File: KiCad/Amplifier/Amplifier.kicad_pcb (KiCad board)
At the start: 2 copper layers, 46 x 56 mm, 29 parts, among them J1 Screw_Terminal_01x03, J2 Screw_Terminal_01x03, Q1 NPN, Q2 NPN, U1 TL074

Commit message: removed unnecessary buffer before filter's output
this drops the number of op amps from 5 to 4, allowing us to use 1 IC instead of 2 ICs with 3 unused circuits.
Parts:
- R10, R9: footprint Resistor_THT:R_Axial_DIN0207_L6.3mm_D2.5mm_P7.62mm_Horizontal -> Resistor_SMD:R_0805_2012Metric
- moved R9 2.99 mm to (83.9, 70.4), turned to 0 degrees
- moved R10 2.79 mm to (83.9, 60.3), turned to 0 degrees
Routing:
- net -9V: track 60.1 -> 53.8 mm
- net GND: track 12.0 -> 16.0 mm, vias 2 -> 4
- net Net-(D2-K): track 4.66 -> 3.01 mm
- net Net-(D1-K): track 3.52 -> 4.19 mm

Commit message: filter pcb layout done
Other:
- board text added: "+9V"
- board text added: "-9V"
- board text added: "Amplifier"
- board text removed: "Oscillator"
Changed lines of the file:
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@@
 			(font
 				(size 1 1)
-				(thickness 0.12)
+				(thickness 0.15)
 			)
 			(justify left bottom)
@@
 			(font
 				(size 1 1)
-				(thickness 0.12)
+				(thickness 0.15)
 			)
 			(justify left bottom)
@@
 			(font
 				(size 1 1)
-				(thickness 0.12)
+				(thickness 0.15)
+			)
+			(justify left bottom)
+		)
+	)
+	(gr_text "-9V"
+		(at 75.5 57 0)
+		(layer "F.SilkS")
+		(effects
+			(font
+				(size 1 1)
+				(thickness 0.15)
+			)
+			(justify left bottom)
+		)
+	)
+	(gr_text "+9V"
+		(at 75.5 72 0)
+		(layer "F.SilkS")
+		(effects
+			(font
+				(size 1 1)
+				(thickness 0.15)
 			)
 			(justify left bottom)
@@
 			(font
 				(size 1 1)
-				(thickness 0.12)
+				(thickness 0.15)
 			)
 			(justify left bottom)
 		)
 	)
-	(gr_text "Oscillator"
-		(at 47.4 70.8 90)
+	(gr_text "Amplifier"
+		(at 48.5 73 90)
 		(layer "F.SilkS")
 		(effects
 			(font
-				(size 2 2)
-				(thickness 0.23)
+				(size 3 3)
+				(thickness 0.45)
 			)
 			(justify left bottom)

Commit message: oscillator pcb layout done
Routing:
- net +9V: track 41.4 -> 46.5 mm
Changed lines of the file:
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@@
+	)
+	(segment
+		(start 73 69)
+		(end 74.5 67.5)
+		(width 0.5)
+		(layer "F.Cu")
+		(net "+9V")
+	)
+	(segment
+		(start 74.5 67.5)
+		(end 77.46 67.5)
+		(width 0.5)
+		(layer "F.Cu")
+		(net "+9V")
 	)
 	(segment

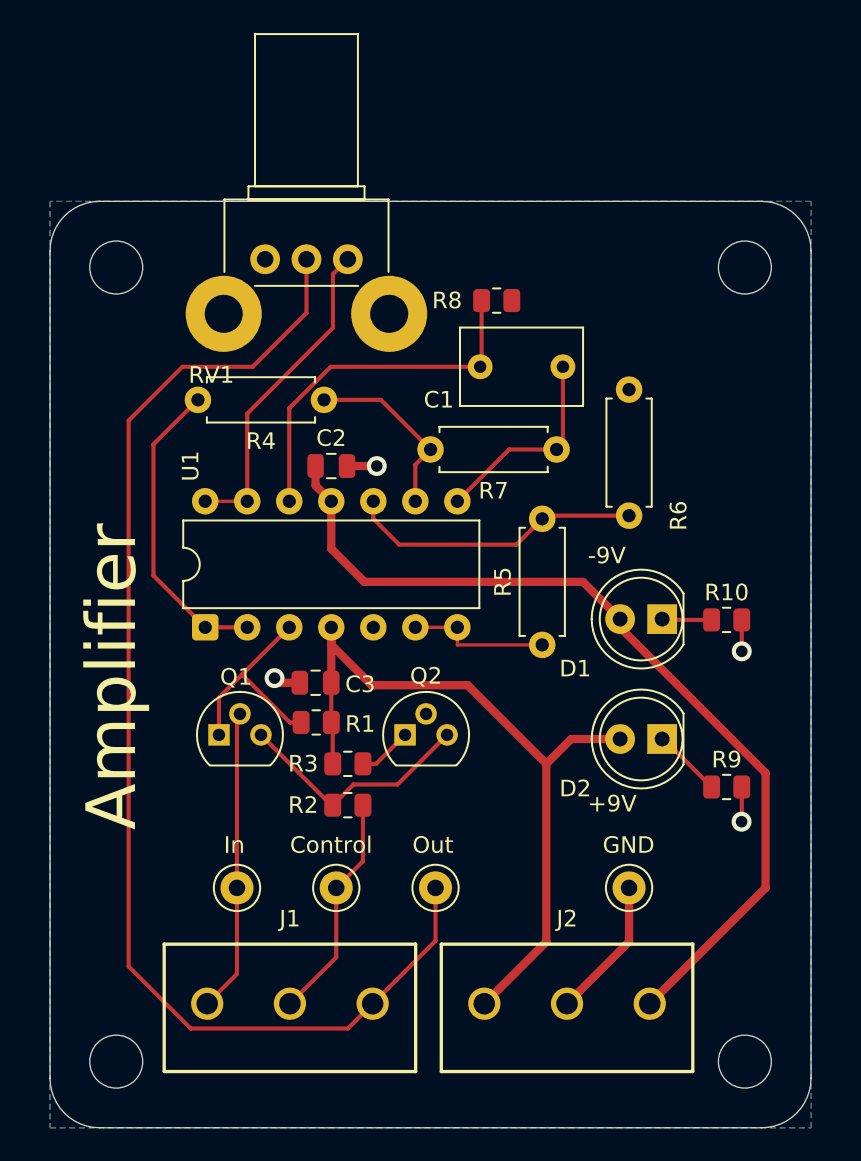
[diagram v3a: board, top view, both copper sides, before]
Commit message: power pcb layout done
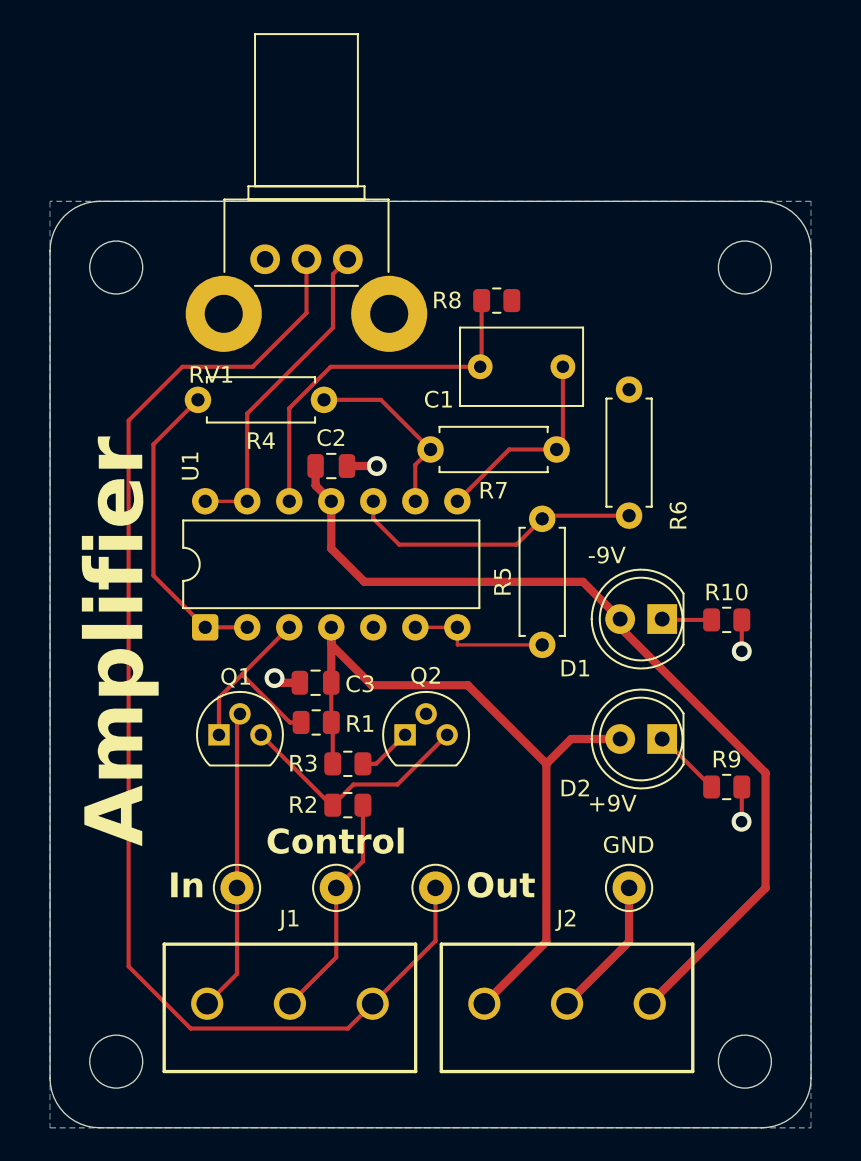
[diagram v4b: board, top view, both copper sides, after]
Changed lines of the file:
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@@
 		(layer "Edge.Cuts")
-	)
-	(gr_text "In"
-		(at 53.5 74.5 0)
-		(layer "F.SilkS")
-		(effects
-			(font
-				(size 1 1)
-				(thickness 0.15)
-			)
-			(justify left bottom)
-		)
-	)
-	(gr_text "Control"
-		(at 57.5 74.5 0)
-		(layer "F.SilkS")
-		(effects
-			(font
-				(size 1 1)
-				(thickness 0.15)
-			)
-			(justify left bottom)
-		)
-	)
-	(gr_text "Out"
-		(at 64.9 74.5 0)
-		(layer "F.SilkS")
-		(effects
-			(font
-				(size 1 1)
-				(thickness 0.15)
-			)
-			(justify left bottom)
-		)
 	)
 	(gr_text "-9V"
@@
 		)
 	)
-	(gr_text "Amplifier"
-		(at 48.5 73 90)
+	(gr_text "In"
+		(at 51.25 77.25 0)
 		(layer "F.SilkS")
 		(effects
 			(font
-				(size 3 3)
-				(thickness 0.45)
+				(size 1.5 1.5)
+				(thickness 0.3)
+				(bold yes)
+			)
+			(justify bottom)
+		)
+	)
+	(gr_text "Control"
+		(at 60.3 74.6 0)
+		(layer "F.SilkS")
+		(effects
+			(font
+				(size 1.5 1.5)
+				(thickness 0.3)
+				(bold yes)
+			)
+			(justify bottom)
+		)
+	)
+	(gr_text "Out"
+		(at 70.25 77.25 0)
+		(layer "F.SilkS")
+		(effects
+			(font
+				(size 1.5 1.5)
+				(thickness 0.3)
+				(bold yes)
+			)
+			(justify bottom)
+		)
+	)
+	(gr_text "Amplifier"
+		(at 49 74 90)
+		(layer "F.SilkS")
+		(effects
+			(font
+				(size 3.5 3.5)
+				(thickness 0.7)
+				(bold yes)
 			)
 			(justify left bottom)

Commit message: added mounting holes to schematics, adjusted board sizes
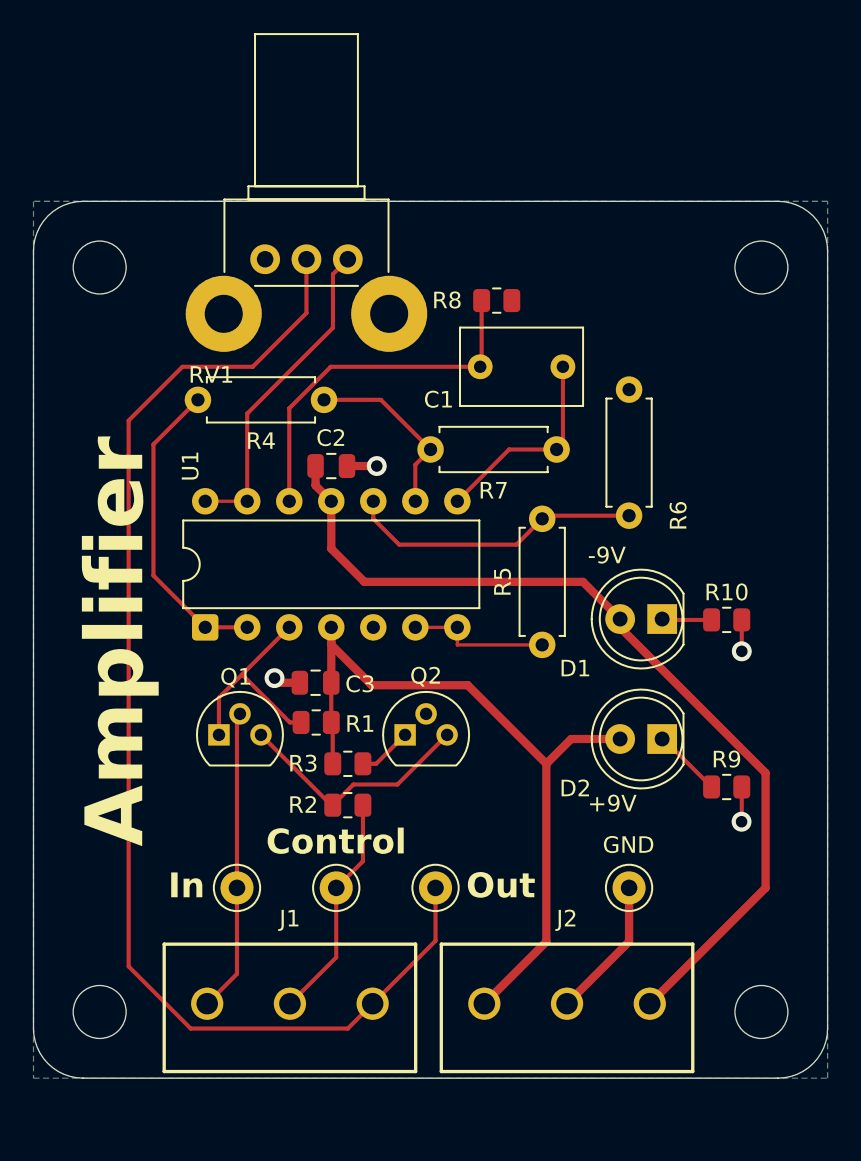
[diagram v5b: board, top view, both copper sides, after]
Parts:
- moved H2 3.16 mm to (46.0, 84.0)
- moved H3 3.16 mm to (86.0, 84.0)
- moved H1 1.00 mm to (46.0, 39.0)
- moved H4 1.00 mm to (86.0, 39.0)
- renumbered REF** to H1, REF** to H2, REF** to H3, REF** to H4
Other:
- board size 46 x 56 mm -> 48 x 53 mm
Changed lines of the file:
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@@
 	(footprint "MountingHole:MountingHole_3.2mm_M3"
 		(layer "F.Cu")
-		(at 47 87)
+		(at 46 84)
 		(descr "Mounting Hole 3.2mm, M3, no annular, generated by kicad-footprint-generator mountinghole.py")
 		(tags "mountinghole M3")
-		(property "Reference" "REF**"
+		(property "Reference" "H2"
 			(at 0 -4.15 0)
 			(layer "F.SilkS")
@@
 	(footprint "MountingHole:MountingHole_3.2mm_M3"
 		(layer "F.Cu")
-		(at 85 39)
+		(at 86 39)
 		(descr "Mounting Hole 3.2mm, M3, no annular, generated by kicad-footprint-generator mountinghole.py")
 		(tags "mountinghole M3")
-		(property "Reference" "REF**"
+		(property "Reference" "H4"
 			(at 0 -4.15 0)
 			(layer "F.SilkS")
@@
 	(footprint "MountingHole:MountingHole_3.2mm_M3"
 		(layer "F.Cu")
-		(at 85 87)
+		(at 86 84)
 		(descr "Mounting Hole 3.2mm, M3, no annular, generated by kicad-footprint-generator mountinghole.py")
 		(tags "mountinghole M3")
-		(property "Reference" "REF**"
+		(property "Reference" "H3"
 			(at 0 -4.15 0)
 			(layer "F.SilkS")
@@
 	(footprint "MountingHole:MountingHole_3.2mm_M3"
 		(layer "F.Cu")
-		(at 47 39)
+		(at 46 39)
 		(descr "Mounting Hole 3.2mm, M3, no annular, generated by kicad-footprint-generator mountinghole.py")
 		(tags "mountinghole M3")
-		(property "Reference" "REF**"
+		(property "Reference" "H1"
 			(at 0 -4.15 0)
 			(layer "F.SilkS")
@@
 	)
 	(gr_line
-		(start 43 88)
-		(end 43.00002 38)
+		(start 42.000001 85)
+		(end 42.00002 38)
 		(stroke
 			(width 0.05)
@@
 	)
 	(gr_arc
-		(start 43.00002 38)
-		(mid 43.8787 35.87868)
-		(end 46.00002 35)
+		(start 42.00002 38)
+		(mid 42.8787 35.87868)
+		(end 45.00002 35)
 		(stroke
 			(width 0.05)
@@
 	)
 	(gr_line
-		(start 46 91)
-		(end 85.999978 91.000002)
+		(start 45 35)
+		(end 86.999997 35.000005)
 		(stroke
 			(width 0.05)
@@
 	)
 	(gr_arc
-		(start 46.000001 91.000017)
-		(mid 43.878681 90.121337)
-		(end 43.000001 88.000017)
+		(start 45.000001 88.000017)
+		(mid 42.878681 87.121337)
+		(end 42.000001 85.000017)
 		(stroke
 			(width 0.05)
@@
 	)
 	(gr_line
-		(start 46.00002 35)
-		(end 85.999998 35.000002)
+		(start 45.000001 88.000017)
+		(end 87 88)
 		(stroke
 			(width 0.05)
@@
 	)
 	(gr_arc
-		(start 85.999997 35.000005)
-		(mid 88.121317 35.878685)
-		(end 88.999997 38.000005)
+		(start 86.999997 35.000005)
+		(mid 89.121317 35.878685)
+		(end 89.999997 38.000005)
 		(stroke
 			(width 0.05)
@@
 	)
 	(gr_arc
-		(start 88.999999 87.999999)
-		(mid 88.121319 90.121319)
-		(end 85.999999 90.999999)
+		(start 89.999999 84.999999)
+		(mid 89.121319 87.121319)
+		(end 86.999999 87.999999)
 		(stroke
 			(width 0.05)
@@
 	)
 	(gr_line
-		(start 88.999999 87.999999)
-		(end 88.999999 37.999999)
+		(start 90 85)
+		(end 89.999999 38)
 		(stroke
 			(width 0.05)
@@
 		(polygon
 			(pts
-				(xy 43 35) (xy 43 91) (xy 89 91) (xy 89 35)
+				(xy 42 35) (xy 42 88) (xy 90 88) (xy 90 35)
 			)
 		)
